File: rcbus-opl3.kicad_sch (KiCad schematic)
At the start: 37 parts, among them CON1 SJ1-3523N, P1 RC2014 BUS, U1 74HCT688, U2 YMF262, U3 YAC512, U4 TL074, Y1 SG-8002CA

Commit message: rename to rcbus-opl3
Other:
- title: RCBUS YMF262 sound card -> RCBUS OPL3 sound card
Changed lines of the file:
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@@
 	(paper "A3")
 	(title_block
-		(title "RCBUS YMF262 sound card")
+		(title "RCBUS OPL3 sound card")
 		(date "${DATE}")
 		(rev "${VERSION}")

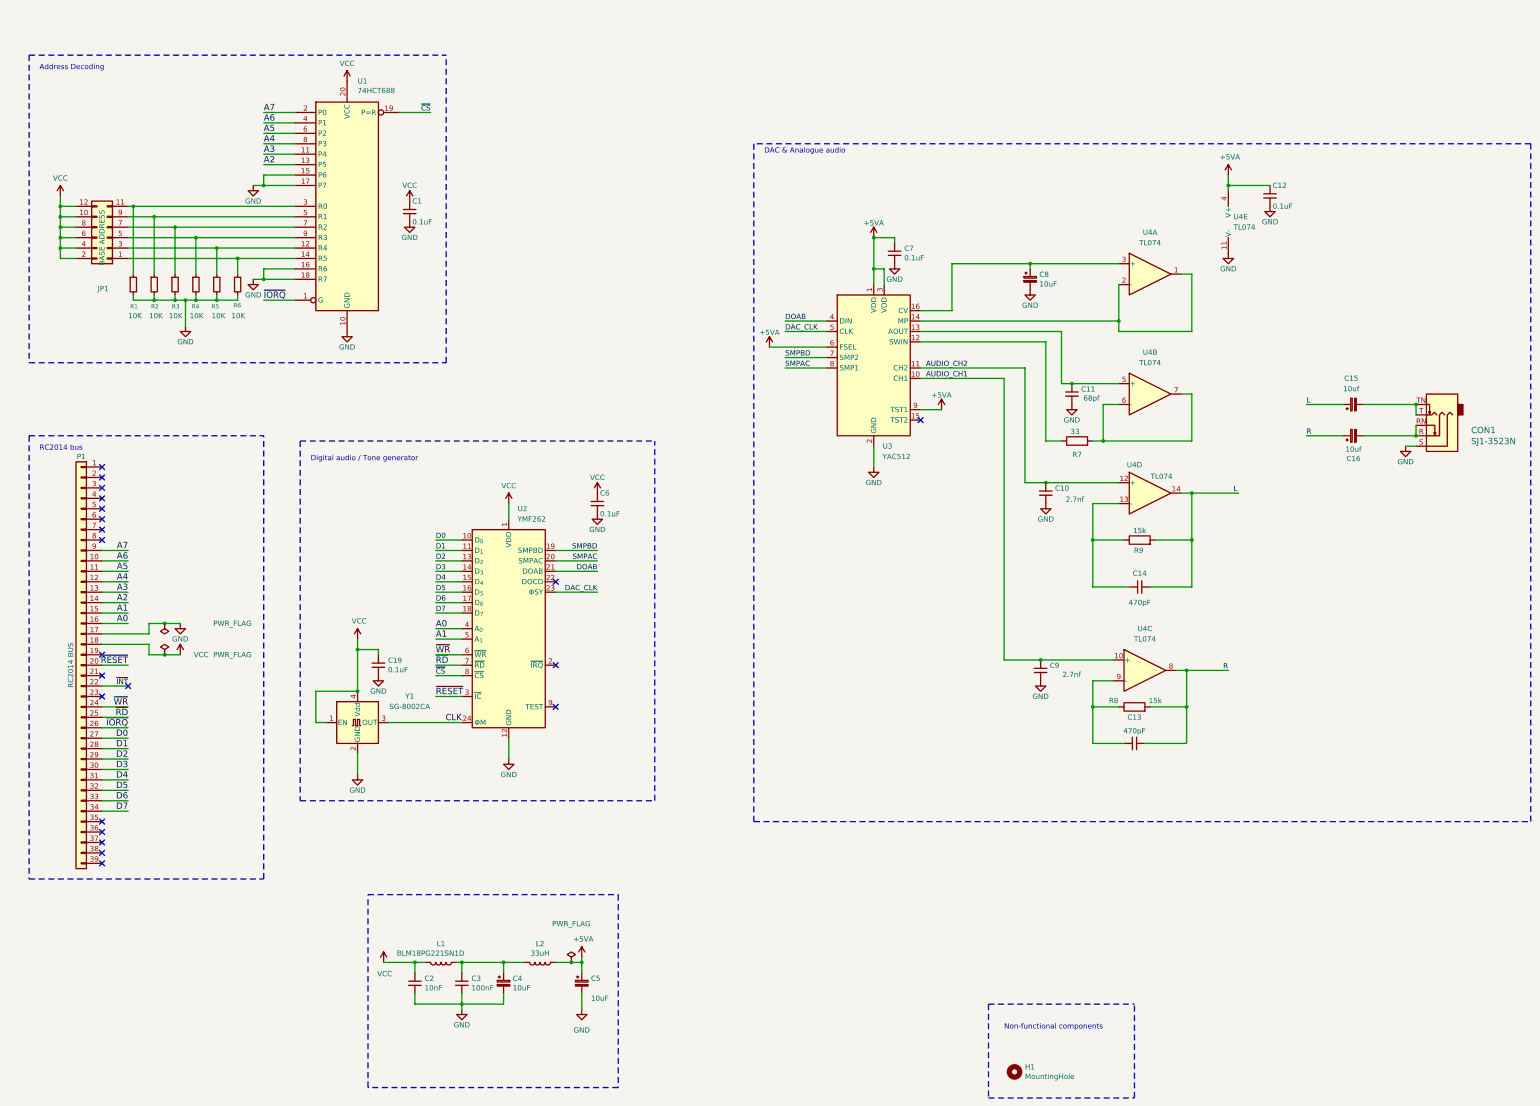
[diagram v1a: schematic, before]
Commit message: remove unneeded components, some layour rejigging
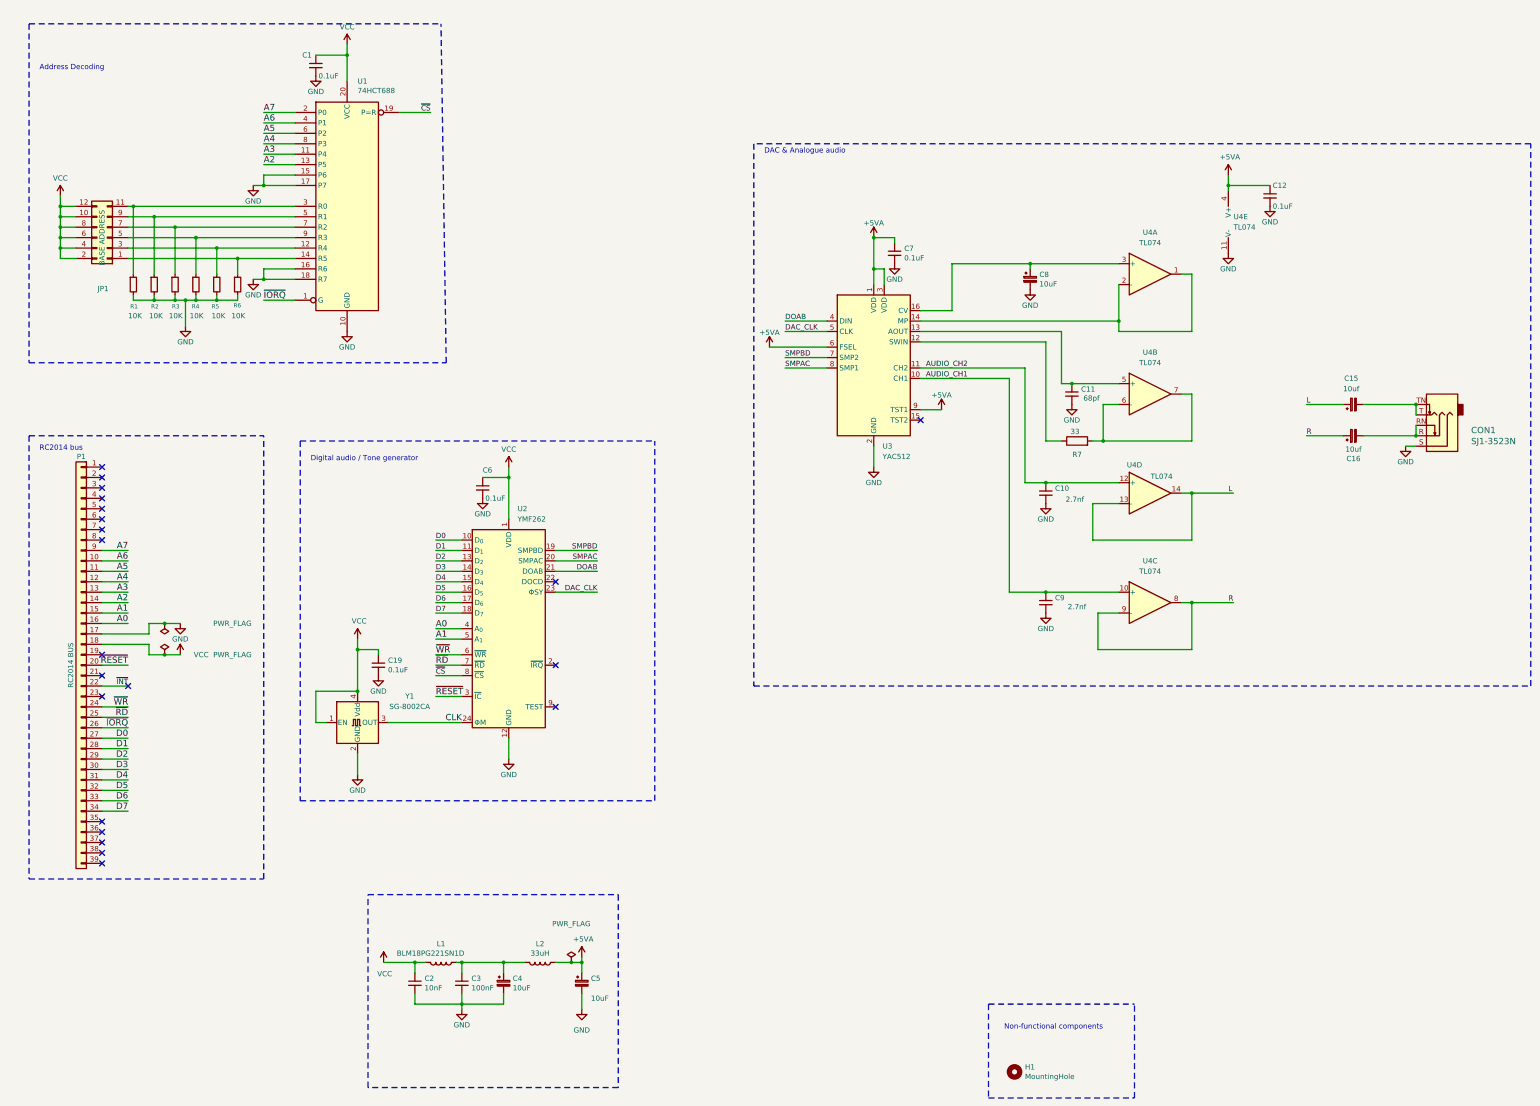
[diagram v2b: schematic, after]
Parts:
- removed C13, C14: 470pF, Capacitor_SMD:C_0603_1608Metric, symbol Device:C_Small
- removed R8, R9: 15k, Resistor_SMD:R_0603_1608Metric, symbol Device:R
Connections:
- net L: now also U4.13 (-)
- net R: now also U4.9 (-)
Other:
- moved on the sheet: C1, C6, C9, U4C

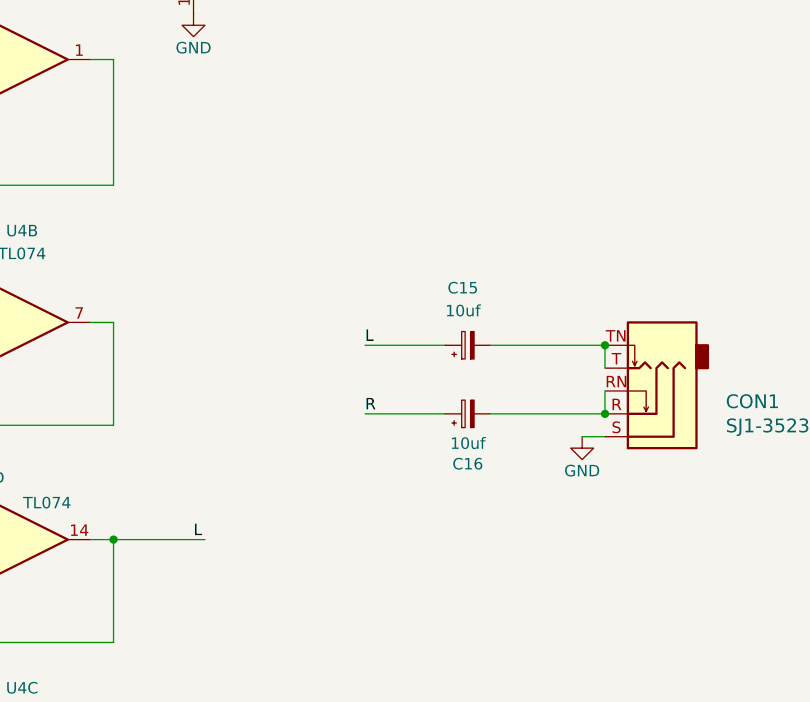
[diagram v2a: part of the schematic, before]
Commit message: add additional output caps/ resistors
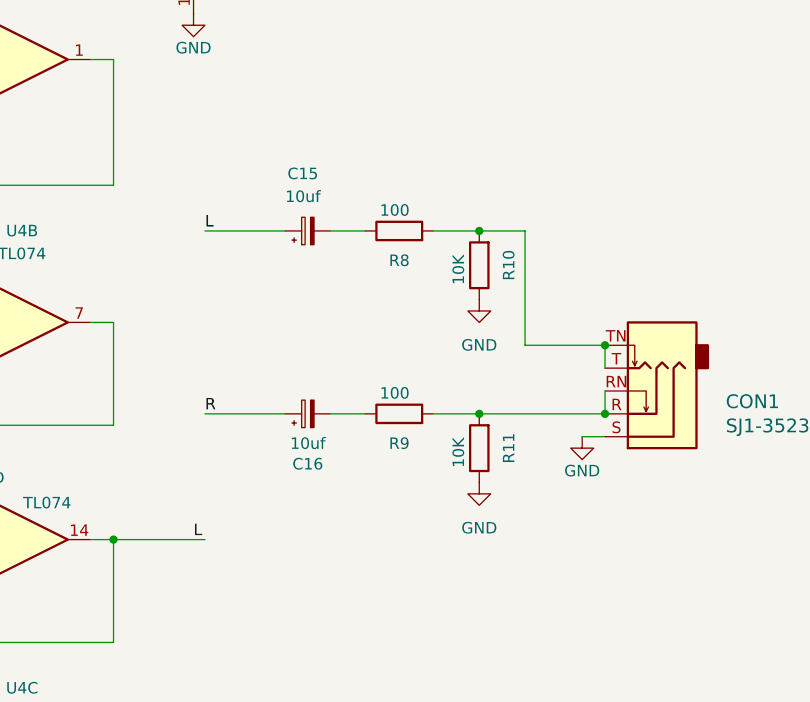
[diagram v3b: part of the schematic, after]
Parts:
- added R10, R11: 10K, Resistor_SMD:R_0603_1608Metric, symbol Device:R
- added R8, R9: 100, Resistor_SMD:R_0603_1608Metric, symbol Device:R
- C15, C16: footprint Capacitor_SMD:C_1206_3216Metric -> Capacitor_SMD:CP_Elec_5x5.9
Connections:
- net GND: now also R10.1, R11.1
- net at CON1.R, CON1.RN: now also R11.2, R9.2; no longer C16.2
- net at CON1.T, CON1.TN: now also R10.2, R8.2; no longer C15.2
- new net: C15.2, R8.1
- new net: C16.2, R9.1
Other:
- moved on the sheet: C15, C16

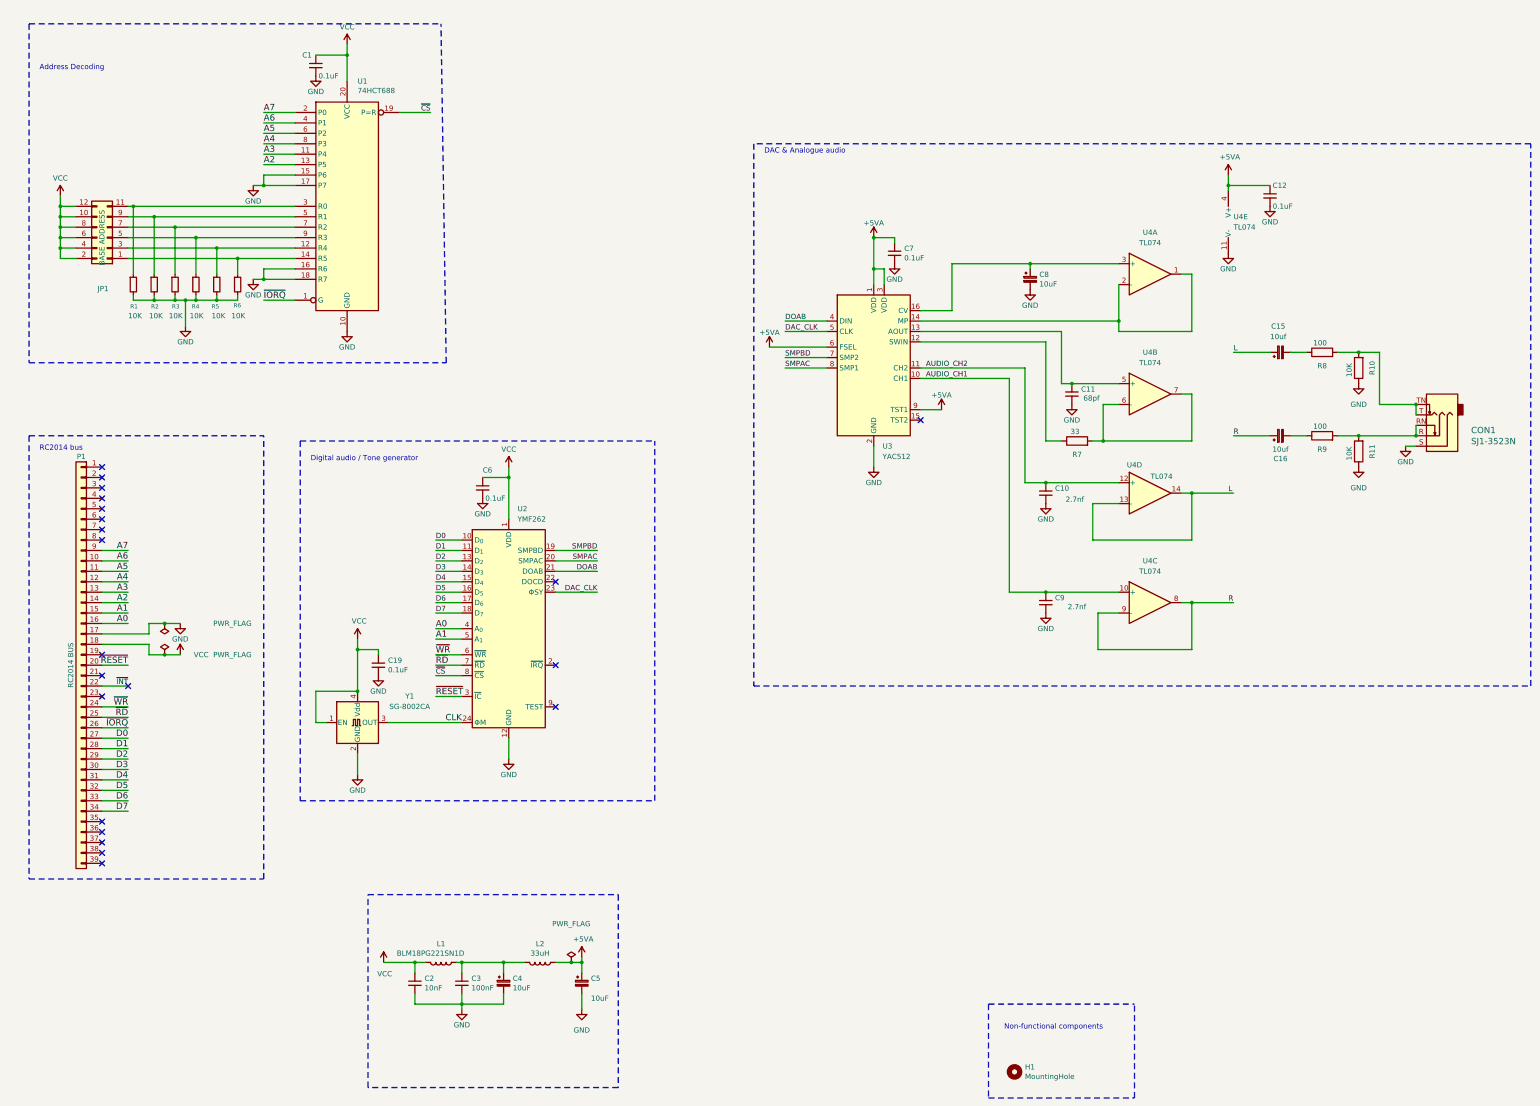
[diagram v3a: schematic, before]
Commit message: remove some unusted stuff from kibot, update schematic and pcb
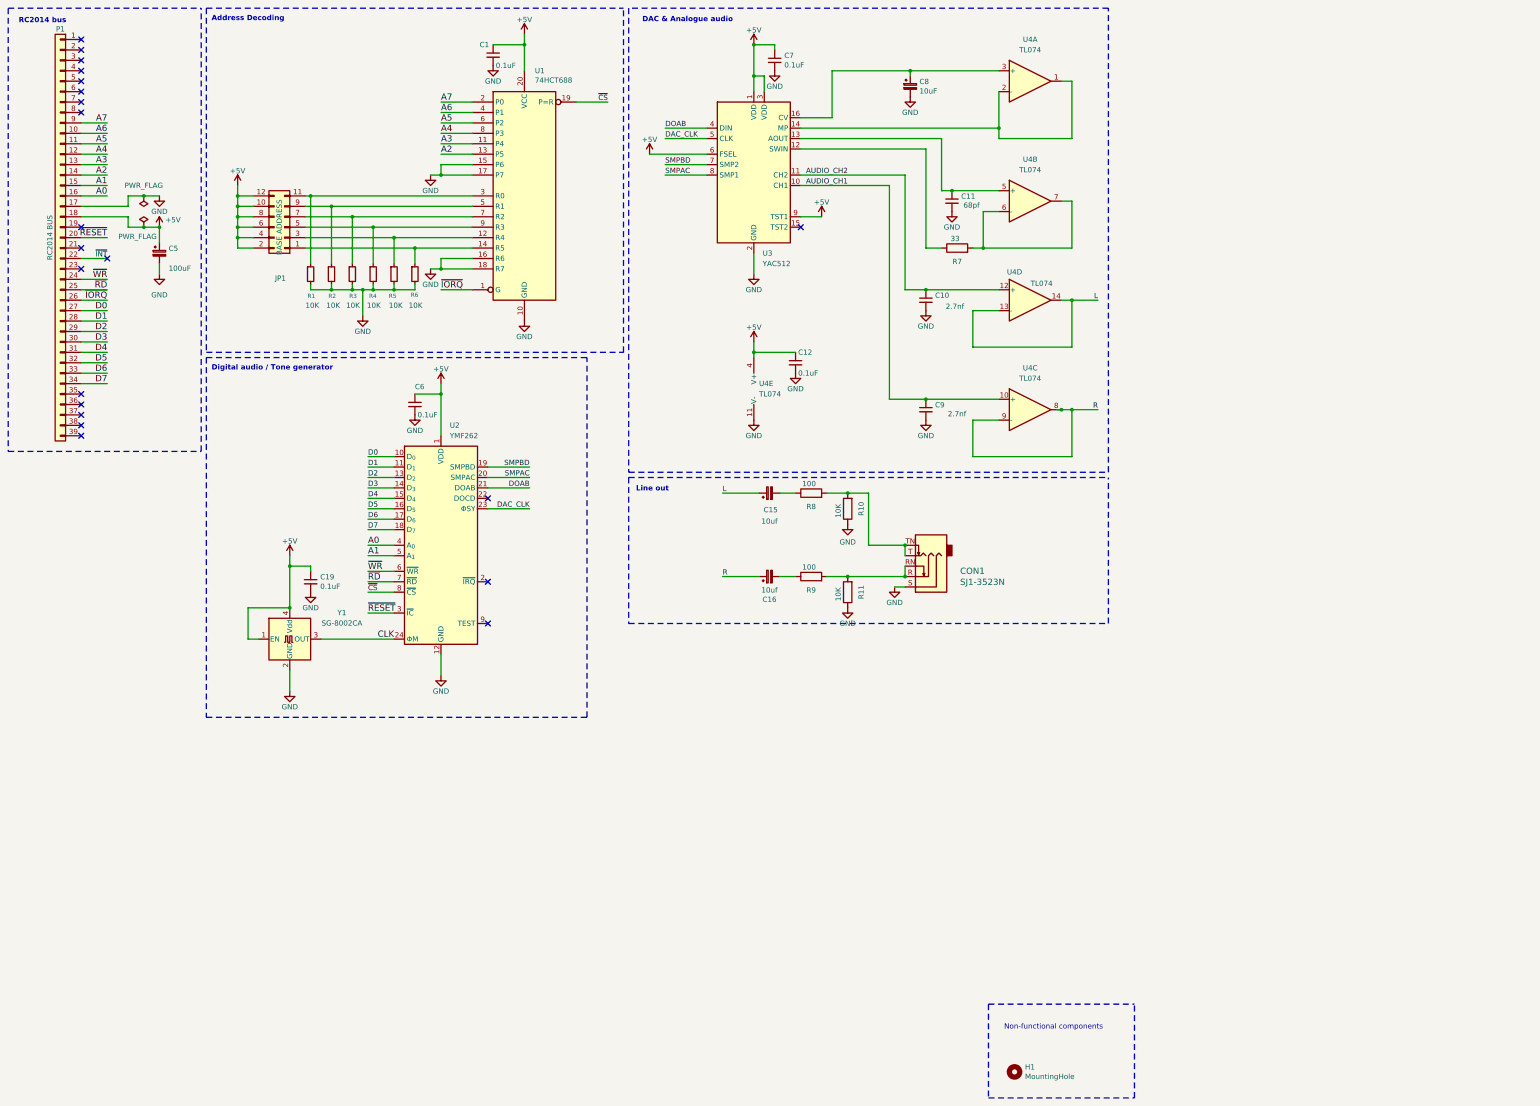
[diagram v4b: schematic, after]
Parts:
- removed C2: 10nF, Capacitor_SMD:C_0603_1608Metric, symbol Device:C_Small
- removed C3: 100nF, Capacitor_SMD:C_0603_1608Metric, symbol Device:C_Small
- removed C4: 10uF, Capacitor_SMD:C_1206_3216Metric, symbol Device:C_Polarized_Small
- removed L1: BLM18PG221SN1D, Inductor_SMD:L_0603_1608Metric, symbol Device:L
- removed L2: 33uH, Inductor_SMD:L_0603_1608Metric, symbol Device:L
- C15, C16: footprint Capacitor_SMD:CP_Elec_5x5.9 -> Capacitor_SMD:CP_Elec_6.3x5.8
- C5: value 10uF -> 100uF; footprint Capacitor_SMD:C_1206_3216Metric -> Capacitor_SMD:CP_Elec_6.3x7.7
- C8: footprint Capacitor_SMD:C_0603_1608Metric -> Capacitor_SMD:CP_Elec_6.3x5.8
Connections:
- net VCC is gone; now on net +5V: C1.1, C19.1, C6.1, JP1.10 (Pin_10), JP1.12 (Pin_12), JP1.2 (Pin_2), JP1.4 (Pin_4), JP1.6 (Pin_6), JP1.8 (Pin_8), P1.18 (Pin_18), U1.20 (VCC), U2.1 (VDD), Y1.1 (EN), Y1.4 (Vdd)
- net +5VA renamed +5V
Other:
- note added: "Line out"
- moved on the sheet: C1, C10, C11, C12, C15, C16, C19, C5, C6, C7, C8, C9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

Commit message: reroute. add additional bulk cap
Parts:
- added C2: 10uf, Capacitor_SMD:CP_Elec_6.3x5.8, symbol Device:C_Polarized_Small
- CON1: value SJ1-3523N -> 3.5mm jack
- Y1: value SG-8002CA -> 14.3181MHz
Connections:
- net +5V: now also C2.1
- net GND: now also C2.2
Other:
- moved on the sheet: C5
